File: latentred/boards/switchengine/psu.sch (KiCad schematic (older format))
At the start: 0 parts

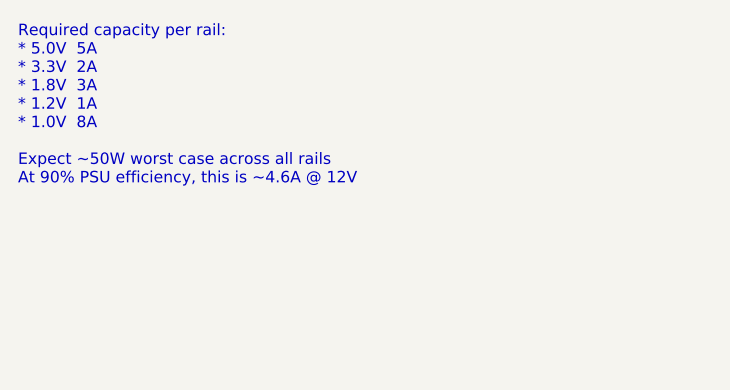
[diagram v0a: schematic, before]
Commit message: Continued initial work on switch engine schematic and power budgeting
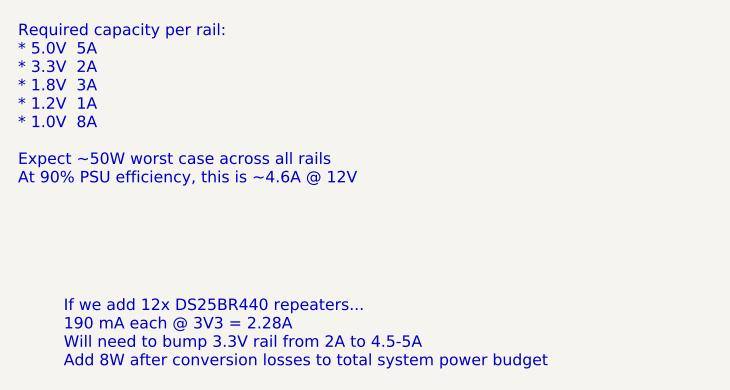
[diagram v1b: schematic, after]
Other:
- note added: "If we add 12x DS25BR440 repeaters...\n190 mA each @ 3V3 = 2.28A\nWill need to bump 3.3V rail from 2A to 4.5-5A\nAdd 8W after conversion losses to total system power budget"
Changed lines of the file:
@@
 $Descr A4 11693 8268
 encoding utf-8
-Sheet 2 5
-Title ""
-Date ""
-Rev ""
-Comp ""
+Sheet 2 6
+Title "LATENTRED Switch Engine"
+Date "2019-09-09"
+Rev "0.1"
+Comp "Antikernel Labs"
 Comment1 ""
-Comment2 ""
+Comment2 "Andrew D. Zonenberg"
 Comment3 ""
 Comment4 ""
@@
 Text Notes 2100 1700 0    50   ~ 0
 Required capacity per rail:\n* 5.0V  5A\n* 3.3V  2A\n* 1.8V  3A\n* 1.2V  1A\n* 1.0V  8A\n\nExpect ~~50W worst case across all rails\nAt 90% PSU efficiency, this is ~~4.6A @ 12V
+Text Notes 2300 2500 0    50   ~ 0
+If we add 12x DS25BR440 repeaters...\n190 mA each @ 3V3 = 2.28A\nWill need to bump 3.3V rail from 2A to 4.5-5A\nAdd 8W after conversion losses to total system power budget
 $EndSCHEMATC
